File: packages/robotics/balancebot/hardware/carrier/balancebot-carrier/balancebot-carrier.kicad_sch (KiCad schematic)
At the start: 19 parts, among them J1 XT30 pack in, J2 LM2596 module, J3 GY-521 MPU6050, J4 Motor left, J5 Motor right, U1 XIAO RP2350

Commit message: feat(balancebot): route the carrier PCB, with build and check recipes
The board is generated from the schematic: build_board.py places the
parts from a table and takes nets from KiCad's netlist export;
route_board.py autoroutes with Freerouting 2.5.0 in three width classes
(1.0 mm VBAT/GND/motor coils, 0.5 mm logic rails, 0.3 mm signals) and
pours GND on both layers. DRC with schematic parity is clean, with no
unconnected items.

Fixes found while routing:
- J1 polarity: KiCad's XT30PW-M footprint prints "-" beside pad 1, so
  pin 1 is now GND and pin 2 VBAT. The first schematic had them swapped.
- XIAO footprint: Seeed's DIP footprint mills a cutout under the module
  and plates holes for its bottom pads. derive_xiao_socket.py makes a
  14-pad socket footprint and matching symbol from it; Seeed's files stay
  unmodified beside them.
- Mounting holes are excluded from the BOM, and FAULT/unused pins carry
  their single-pin nets, so schematic parity has no findings.

check_pins.py ties the board to the firmware: every role in
src/pin_config.h must land on the carrier net meant for it, read through
the hardware join. Moving PIN_DIR_LEFT to GPIO27 fails it.

just balancebot::carrier-{lib,board,check,fab}; carrier-fab writes the
JLCPCB Gerber/drill zip after running the checks.

Co-Authored-By: Claude Opus 5.5 <noreply@anthropic.com>
Claude-Session: https://claude.ai/code/session_01UTpEnVq88KD8afKQoLqdyC
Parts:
- removed U1: XIAO RP2350, Seeed_XIAO:XIAO-RP2350-DIP, symbol Seeed_XIAO:XIAO-RP2350-DIP
- added U1: XIAO RP2350, Seeed_XIAO:XIAO-RP2350-Socket, symbol Seeed_XIAO:XIAO-RP2350-Socket
- H1, H2, H3, H4: now left out of the parts list
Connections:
- net +3V3: now also U1.12 (3V3_OUT)
- net DIR_L: now also U1.10 (D9)
- net DIR_R: now also U1.7 (D6)
- net GND: now also J1.1 (Pin_1), U1.13 (GND); no longer J1.2 (Pin_2)
- net IMU_INT: now also U1.4 (D3)
- net IMU_SCL: now also U1.6 (D5)
- net IMU_SDA: now also U1.5 (D4)
- net NENABLE: now also U1.8 (D7)
- net PACK_SENSE: now also U1.1 (D0)
- net STEP_L: now also U1.9 (D8)
- net STEP_R: now also U1.11 (D10)
- net VBAT: now also J1.2 (Pin_2); no longer J1.1 (Pin_1)
- net XIAO_5V: now also U1.14 (VBUS)
- no-connect marks 16 -> 6

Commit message: feat(balancebot): SMD passives on the carrier, with JLCPCB assembly files (#753)
R1-R3 and C3 move to 0805 hand-solder pads, D1 to a B5819W in SOD-123 and
C1/C2 to 100 uF 35 V 6.3x7.7 mm SMD electrolytics. Each symbol carries an
LCSC number (all JLC Basic except C1/C2), so the same board can be
hand-soldered or assembled by JLCPCB; carrier-fab now also writes a
JLC-format BOM and CPL holding only those seven parts. Modules, sockets and
connectors stay through-hole.

build_board.py copies custom symbol fields onto the footprints (hidden, on
F.Fab) so DRC schematic parity holds. The board was regenerated and
rerouted; ERC, DRC (0 violations, 0 unconnected, 0 parity) and the
pin_config.h cross-check pass.


Claude-Session: https://claude.ai/code/session_01UKeVTQabun2jCo4T7rwoBH

Co-authored-by: Claude Opus 5.5 <noreply@anthropic.com>
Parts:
- C1, C2: value 100uF 25V -> 100uF 35V; footprint Capacitor_THT:CP_Radial_D8.0mm_P3.50mm -> Capacitor_SMD:CP_Elec_6.3x7.7; LCSC (none) -> C2836437
- C3: footprint Capacitor_THT:C_Disc_D5.0mm_W2.5mm_P5.00mm -> Capacitor_SMD:C_0805_2012Metric_Pad1.18x1.45mm_HandSolder; LCSC (none) -> C49678
- D1: value 1N5819 -> B5819W; footprint Diode_THT:D_DO-41_SOD81_P10.16mm_Horizontal -> Diode_SMD:D_SOD-123; LCSC (none) -> C8598
- R1: footprint Resistor_THT:R_Axial_DIN0207_L6.3mm_D2.5mm_P10.16mm_Horizontal -> Resistor_SMD:R_0805_2012Metric_Pad1.20x1.40mm_HandSolder; LCSC (none) -> C17414
- R2: footprint Resistor_THT:R_Axial_DIN0207_L6.3mm_D2.5mm_P10.16mm_Horizontal -> Resistor_SMD:R_0805_2012Metric_Pad1.20x1.40mm_HandSolder; LCSC (none) -> C149504
- R3: footprint Resistor_THT:R_Axial_DIN0207_L6.3mm_D2.5mm_P10.16mm_Horizontal -> Resistor_SMD:R_0805_2012Metric_Pad1.20x1.40mm_HandSolder; LCSC (none) -> C17593
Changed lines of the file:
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@@
 			)
 		)
-		(property "Value" "100uF 25V"
+		(property "Value" "100uF 35V"
 			(at 379.73 163.83 0)
 			(show_name no)
@@
 			)
 		)
-		(property "Footprint" "Capacitor_THT:CP_Radial_D8.0mm_P3.50mm"
+		(property "Footprint" "Capacitor_SMD:CP_Elec_6.3x7.7"
+			(at 379.73 160.02 0)
+			(hide yes)
+			(show_name no)
+			(do_not_autoplace no)
+			(effects
+				(font
+					(size 1.27 1.27)
+				)
+			)
+		)
+		(property "LCSC" "C2836437"
 			(at 379.73 160.02 0)
 			(hide yes)
@@
 			)
 		)
-		(property "Footprint" "Resistor_THT:R_Axial_DIN0207_L6.3mm_D2.5mm_P10.16mm_Horizontal"
+		(property "Footprint" "Resistor_SMD:R_0805_2012Metric_Pad1.20x1.40mm_HandSolder"
+			(at 149.86 149.86 0)
+			(hide yes)
+			(show_name no)
+			(do_not_autoplace no)
+			(effects
+				(font
+					(size 1.27 1.27)
+				)
+			)
+		)
+		(property "LCSC" "C149504"
 			(at 149.86 149.86 0)
 			(hide yes)
@@
 			)
 		)
-		(property "Footprint" "Resistor_THT:R_Axial_DIN0207_L6.3mm_D2.5mm_P10.16mm_Horizontal"
+		(property "Footprint" "Resistor_SMD:R_0805_2012Metric_Pad1.20x1.40mm_HandSolder"
+			(at 149.86 180.34 0)
+			(hide yes)
+			(show_name no)
+			(do_not_autoplace no)
+			(effects
+				(font
+					(size 1.27 1.27)
+				)
+			)
+		)
+		(property "LCSC" "C17593"
 			(at 149.86 180.34 0)
 			(hide yes)
@@
 			)
 		)
-		(property "Value" "1N5819"
+		(property "Value" "B5819W"
 			(at 229.87 163.83 0)
 			(show_name no)
@@
 			)
 		)
-		(property "Footprint" "Diode_THT:D_DO-41_SOD81_P10.16mm_Horizontal"
+		(property "Footprint" "Diode_SMD:D_SOD-123"
+			(at 229.87 160.02 0)
+			(hide yes)
+			(show_name no)
+			(do_not_autoplace no)
+			(effects
+				(font
+					(size 1.27 1.27)
+				)
+			)
+		)
+		(property "LCSC" "C8598"
 			(at 229.87 160.02 0)
 			(hide yes)
@@
 			)
 		)
-		(property "Footprint" "Resistor_THT:R_Axial_DIN0207_L6.3mm_D2.5mm_P10.16mm_Horizontal"
+		(property "Footprint" "Resistor_SMD:R_0805_2012Metric_Pad1.20x1.40mm_HandSolder"
+			(at 100.33 160.02 0)
+			(hide yes)
+			(show_name no)
+			(do_not_autoplace no)
+			(effects
+				(font
+					(size 1.27 1.27)
+				)
+			)
+		)
+		(property "LCSC" "C17414"
 			(at 100.33 160.02 0)
 			(hide yes)
@@
 			)
 		)
-		(property "Footprint" "Capacitor_THT:C_Disc_D5.0mm_W2.5mm_P5.00mm"
+		(property "Footprint" "Capacitor_SMD:C_0805_2012Metric_Pad1.18x1.45mm_HandSolder"
+			(at 180.34 180.34 0)
+			(hide yes)
+			(show_name no)
+			(do_not_autoplace no)
+			(effects
+				(font
+					(size 1.27 1.27)
+				)
+			)
+		)
+		(property "LCSC" "C49678"
 			(at 180.34 180.34 0)
 			(hide yes)
@@
 			)
 		)
-		(property "Value" "100uF 25V"
+		(property "Value" "100uF 35V"
 			(at 350.52 163.83 0)
 			(show_name no)
@@
 			)
 		)
-		(property "Footprint" "Capacitor_THT:CP_Radial_D8.0mm_P3.50mm"
+		(property "Footprint" "Capacitor_SMD:CP_Elec_6.3x7.7"
 			(at 350.52 160.02 0)
 			(hide yes)
+			(show_name no)
+			(do_not_autoplace no)
+			(effects
+				(font
+					(size 1.27 1.27)
+				)
+			)
+		)
+		(property "LCSC" "C2836437"
+			(at 350.52 160.02 0)
+			(hide yes)

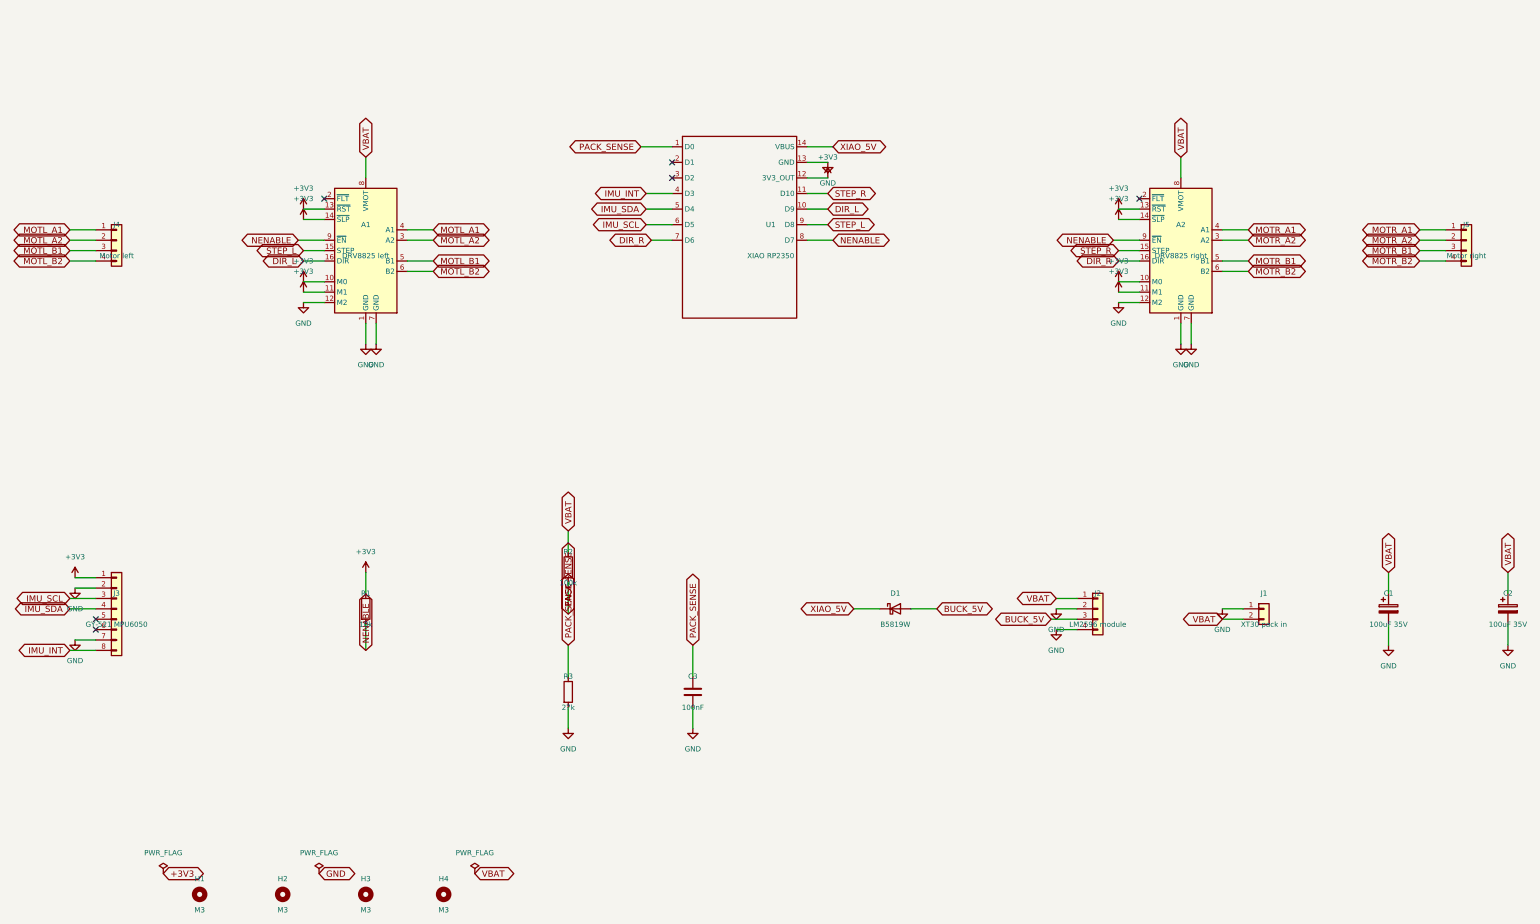
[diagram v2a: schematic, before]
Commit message: feat(kicad): generate the balancebot carrier schematic from the hardware join (#759)
* feat(kicad): vendor the KiCad 10.0.6 symbols and footprints the carriers use

CI must generate and check a carrier board without KiCad installed, and local
ERC/DRC must read the same library bytes CI pins (ADR-027, #750). This adds
the start of tools/kicad and the CC-BY-SA subset it reads.

tools/kicad/lib/kicad-stock/ holds the 10 symbols and 15 footprints the
balancebot carrier and its perfboard stand-ins reference: symbol libraries as
extracted subsets with each block unchanged, footprints as byte copies,
upstream LICENSE.md verbatim, and a README with the attribution and the
modification notice CC-BY-SA 4.0 s3(a)(1)(B) requires. The root README now
says the MIT licence does not cover that directory.

MANIFEST.tsv pins every vendored file's sha256. `kicad.vendor --check`
(KiCad-free) recomputes them and fails on a mismatch, an unlisted or missing
file, a derived (extends) symbol, or any part vendored but not referenced or
referenced but not vendored. The project library tables will point KiCad at
these same files, so a hand edit would otherwise agree with everything
generated from it. `--check-installed` is the informational drift report
against the installed KiCad; `--update` rebuilds the subtree from it.

The library modules (paths, sexpr, library, symbols, footprints) carry the
resolver order of spec s3.4, the lib_symbols embedding KiCad itself writes
(pinned against Device:R from #749's committed schematic), and the shared
project-argument handling that makes every per-project CLI exit 1 on
"0 project(s)" unless given --allow-none.

Until the parts registry lands, vendor.py spells the referenced set; the
registry becomes its source in the next wave.

Co-Authored-By: Claude Opus 5.5 <noreply@anthropic.com>
Claude-Session: https://claude.ai/code/session_01FLEUUmprvHRLXbK9YxaxiY

* refactor(kicad): move the Seeed XIAO library and socket derivation to tools/kicad

The Seeed XIA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
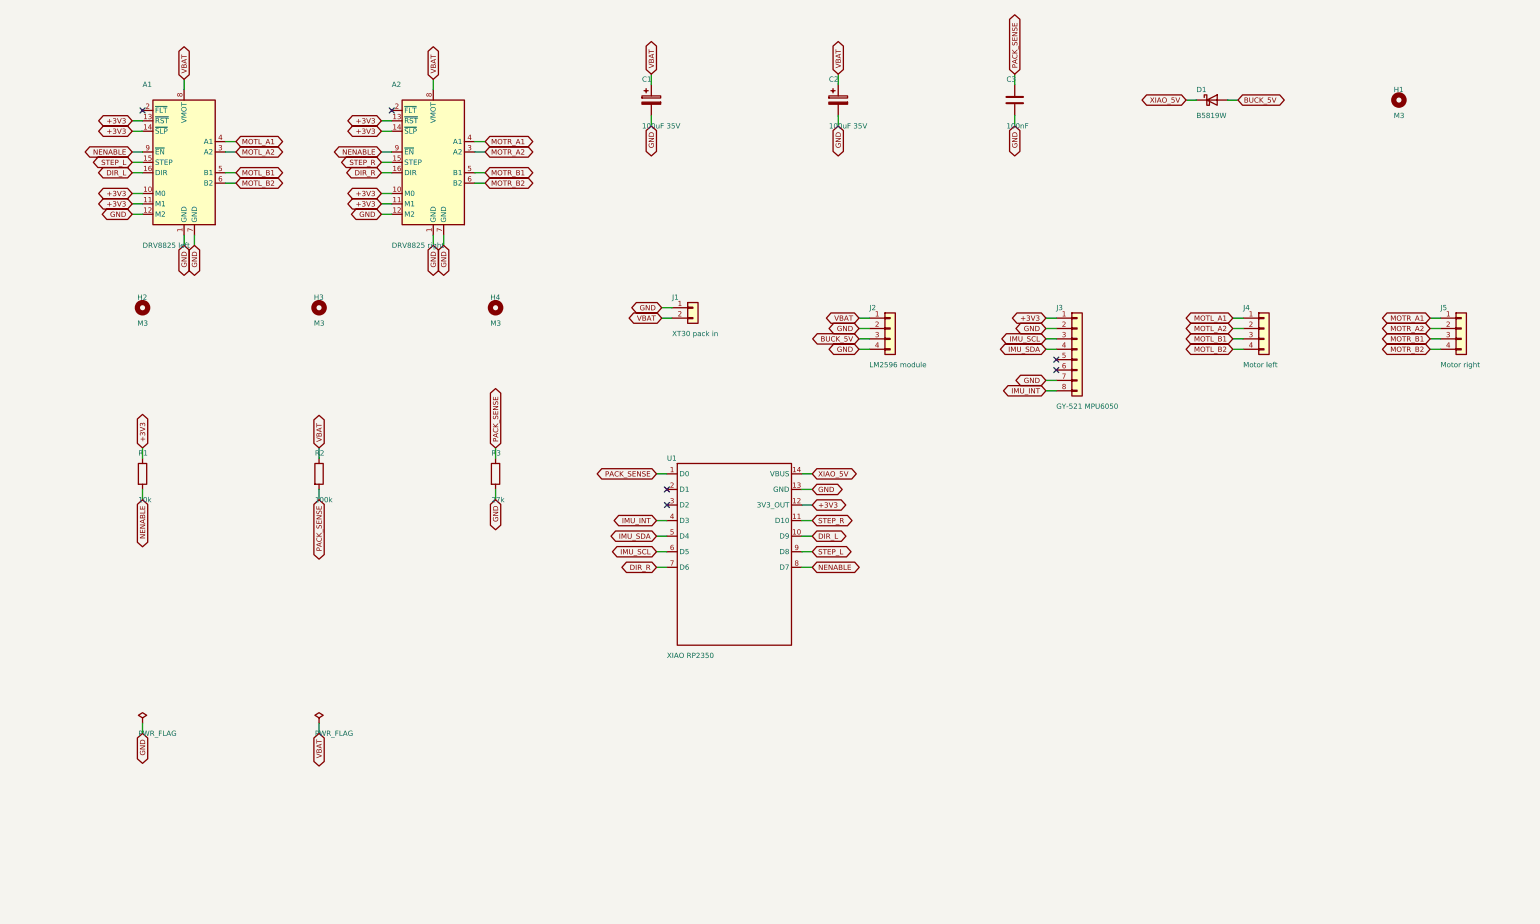
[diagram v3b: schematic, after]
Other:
- title: (none) -> balancebot-carrier

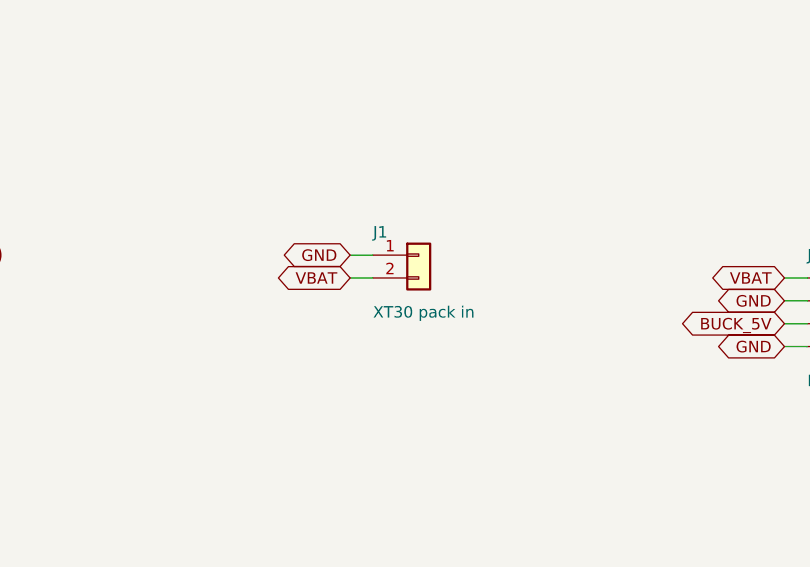
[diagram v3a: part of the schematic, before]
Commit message: fix(balancebot): seat the GY-521 right side up and take the pack on JST-XH (#770)
* fix(balancebot): seat the GY-521 right side up and take the pack on JST-XH

J3 sat at the front edge of the GY-521's outline, so the module hung
rearward from it. Component side up, that put VCC on the wrong end of
the socket; component side down, Z pointed down and the firmware's
atan2(accel_x, accel_z) would read about 180 deg upright. Moving J3 to
the rear edge (y 33 -> 47) puts VCC on pin 1 with the module component
side up, its X arrow toward FWD and Z up, as WIRING.md and the firmware
expect.

The XT30 is replaced by a JST-XH 2-pin (no XT30 plugs on hand). The new
registry entry names its pins BAT+/BAT- rather than +/-: the JST-XH
footprint prints no polarity for the tripwire to prove, so the carrier
silkscreen prints + and - over the pads instead. The XT30 entry and its
vendored footprint stay for the registry tests.

The DRV8825 and GY-521 pin orders in the pre-order checks are confirmed
against the HW-216 carriers and the GY-521 on hand (#748).

Co-Authored-By: Claude Opus 5.5 <noreply@anthropic.com>
Claude-Session: https://claude.ai/code/session_01V4exdSPypzhBpgNeQYJDD5

* docs(parts): record the GY-521 and DRV8825 pin orders as checked

Both were read off the fitted modules on 2026-10-14 (#748); the
registry's source lines still said "from memory" and "not yet checked".
The test_bad_values mutation now anchors on the source key rather than
its old wording.

Co-Authored-By: Claude Opus 5.5 <noreply@anthropic.com>
Claude-Session: https://claude.ai/code/session_01V4exdSPypzhBpgNeQYJDD5

* fix(balancebot): point the perfboard GY-521's X arrow forward

The perfboard socket sat on row 1 with pin 1 at its right end, so the
module, component side up, hung rearward and its X arrow pointed to the
rear, against the README and the firmware's X-forward mounting. The
socket now runs I7-P7 with VCC at I7 and the module extends toward
row 1, matching the carrier's J3.

Co-Authored-By: Cla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
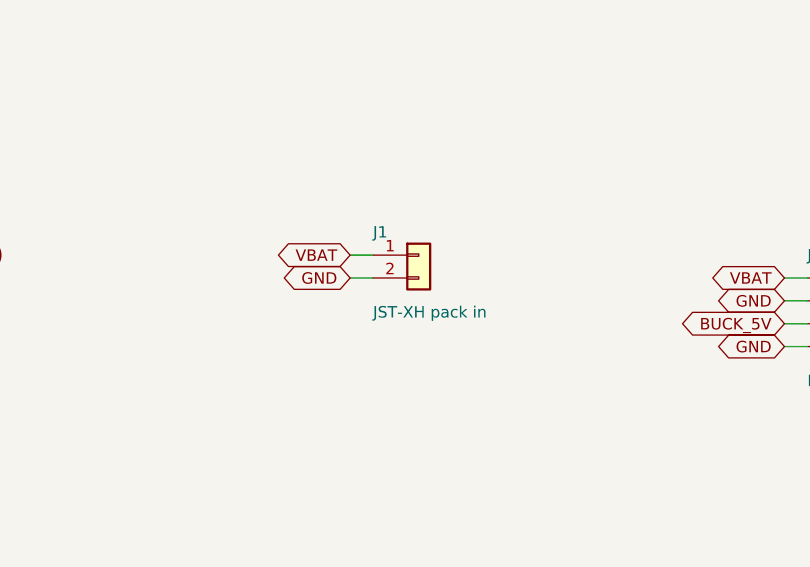
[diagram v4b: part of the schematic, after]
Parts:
- J1: value XT30 pack in -> JST-XH pack in; footprint Connector_AMASS:AMASS_XT30PW-M_1x02_P2.50mm_Horizontal -> Connector_JST:JST_XH_B2B-XH-A_1x02_P2.50mm_Vertical
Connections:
- net GND: now also J1.2 (Pin_2); no longer J1.1 (Pin_1)
- net VBAT: now also J1.1 (Pin_1); no longer J1.2 (Pin_2)
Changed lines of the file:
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@@
 			)
 		)
-		(property "Value" "XT30 pack in"
+		(property "Value" "JST-XH pack in"
 			(at 175.26 92.71 0)
 			(show_name no)
@@
 			)
 		)
-		(property "Footprint" "Connector_AMASS:AMASS_XT30PW-M_1x02_P2.50mm_Horizontal"
+		(property "Footprint" "Connector_JST:JST_XH_B2B-XH-A_1x02_P2.50mm_Vertical"
 			(at 180.34 86.36 0)
 			(hide yes)
@@
 		)
 	)
-	(global_label "GND"
+	(global_label "VBAT"
 		(shape bidirectional)
 		(at 172.72 86.36 180)
@@
 		)
 	)
-	(global_label "VBAT"
+	(global_label "GND"
 		(shape bidirectional)
 		(at 172.72 88.9 180)
